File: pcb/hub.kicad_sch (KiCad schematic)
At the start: 0 parts

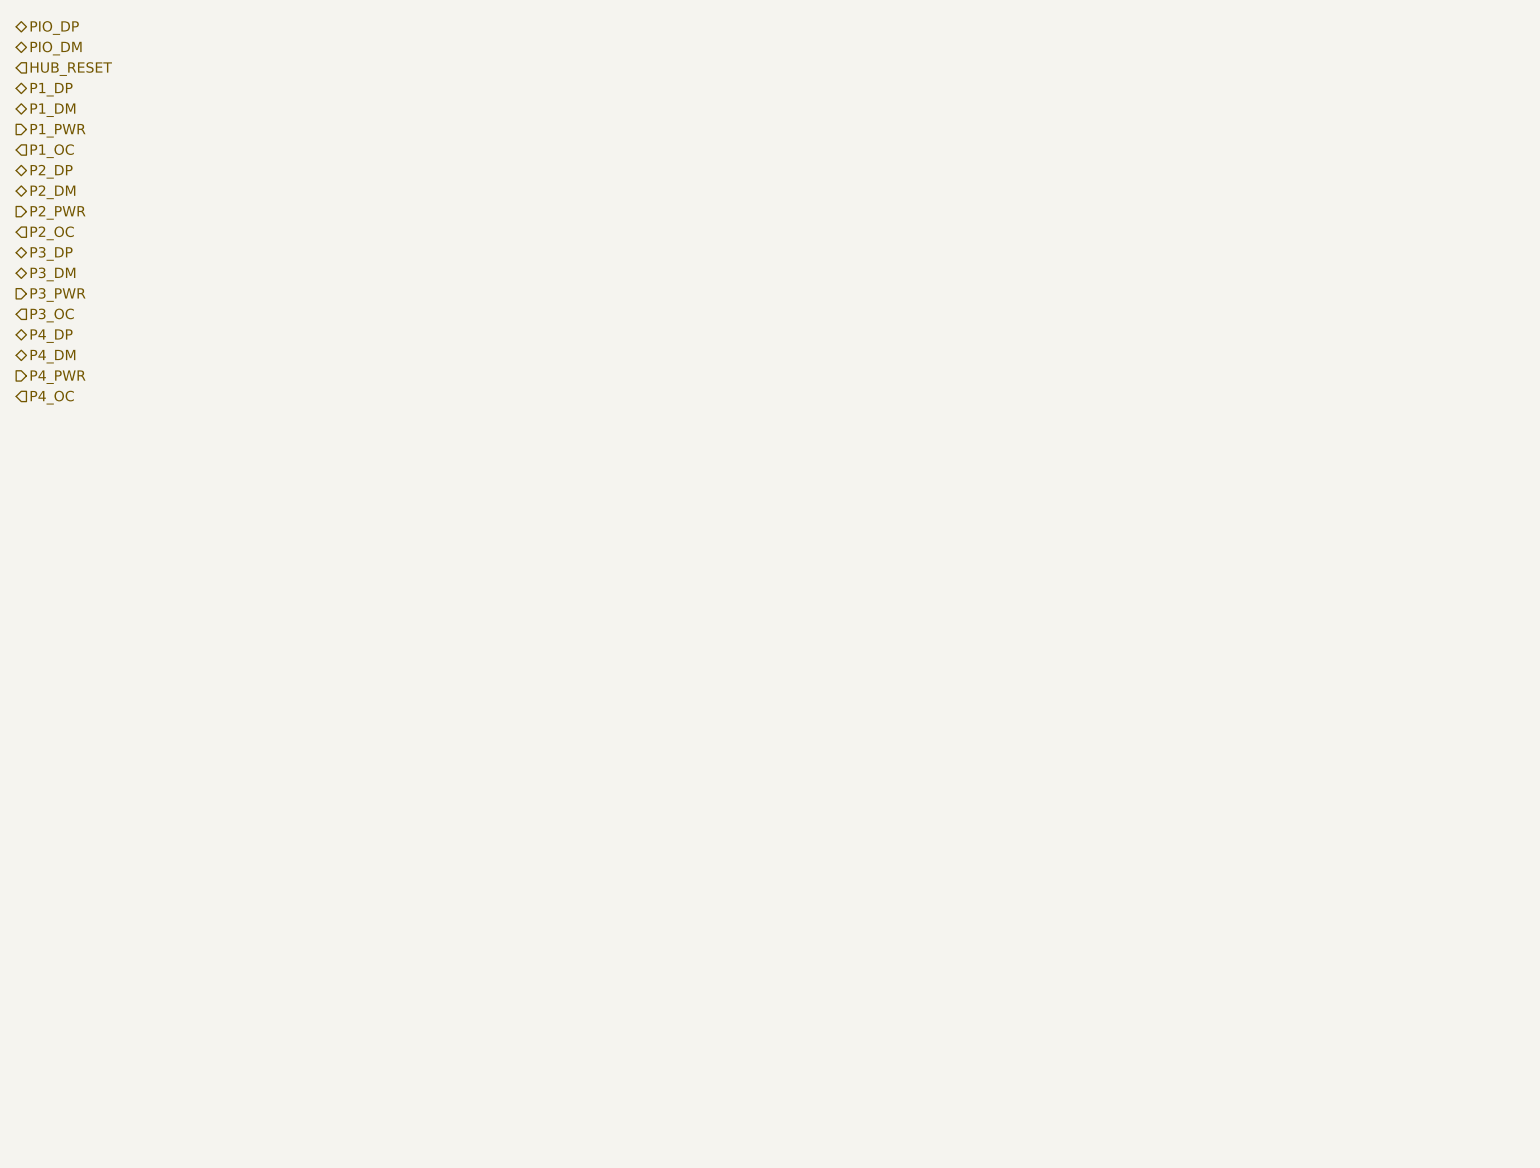
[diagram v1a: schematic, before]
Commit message: draw the hub sheet, with every passive turned side-on
The hub, its 24 MHz crystal, the RBIAS reference, both regulator filters, the
straps that select the default configuration, the reset and upstream-detect
pull-downs, and the upstream pair's series resistors with their host-side
pull-downs.

The thing that makes this sheet readable is that the passives are rotated. A
part standing upright has to be reached by a wire that leaves its pin's row, and
on a chip with fourteen pins down one side those wires cross each other and
everything else. Turned side-on, each passive sits in line with the pin it
serves: every pin owns a row and nothing crosses. The rotation convention was
measured out of KiCad rather than assumed -- a symbol turned 90 degrees puts a
pin at (X - py, Y - px), and the pin's own direction turns with it.

The datasheet settled what hangs off each pin. Both regulator filters take up to
0.1uF to ground or may be left unconnected. RBIAS takes 12.0k at 1%. TEST is to
be left alone -- no trace, no signal. And the two configuration-select pins are
strapped low through resistors rather than tied, because after reset they revert
to other functions, one of them an output.

HUB_VBUS_DET is plumbed through: a sheet pin on both blocks in the root, and on
the MCU sheet a pin that was spare now drives it.

Co-Authored-By: Claude Opus 5 (1M context) <noreply@anthropic.com>
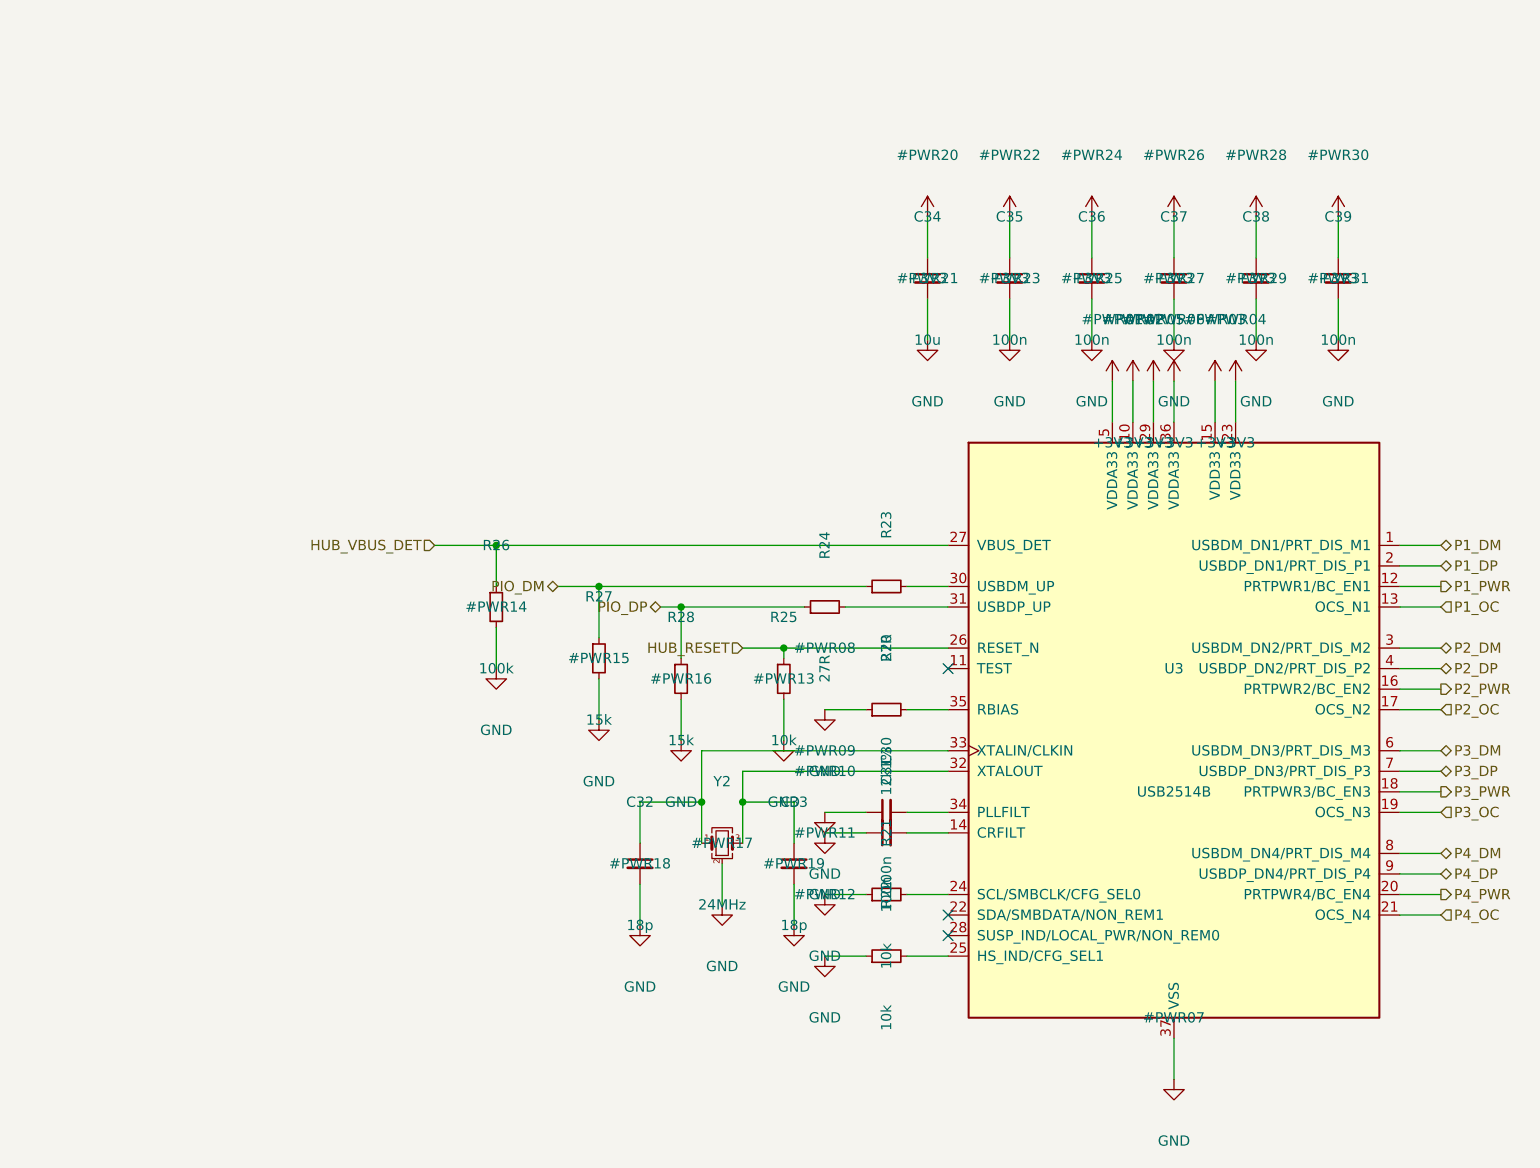
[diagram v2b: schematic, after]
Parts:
- added C30, C31, C35, C36, C37, C38, C39: 100n, symbol Device:C_Small
- added C32, C33: 18p, symbol Device:C_Small
- added C34: 10u, symbol Device:C_Small
- added R20: 12k1%, symbol Device:R_Small
- added R21, R22, R25: 10k, symbol Device:R_Small
- added R23, R24: 27R, symbol Device:R_Small
- added R26: 100k, symbol Device:R_Small
- added R27, R28: 15k, symbol Device:R_Small
- added U3: USB2514B, symbol Interface_USB:USB2514B_Bi
- added Y2: 24MHz, symbol Device:Crystal_GND24_Small
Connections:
- net HUB_RESET: now also R25.1, U3.26 (RESET_N)
- net P1_DM: now also U3.1 (USBDM_DN1/PRT_DIS_M1)
- net P1_DP: now also U3.2 (USBDP_DN1/PRT_DIS_P1)
- net P1_OC: now also U3.13 (OCS_N1)
- net P1_PWR: now also U3.12 (PRTPWR1/BC_EN1)
- net P2_DM: now also U3.3 (USBDM_DN2/PRT_DIS_M2)
- net P2_DP: now also U3.4 (USBDP_DN2/PRT_DIS_P2)
- net P2_OC: now also U3.17 (OCS_N2)
- net P2_PWR: now also U3.16 (PRTPWR2/BC_EN2)
- net P3_DM: now also U3.6 (USBDM_DN3/PRT_DIS_M3)
- net P3_DP: now also U3.7 (USBDP_DN3/PRT_DIS_P3)
- net P3_OC: now also U3.19 (OCS_N3)
- net P3_PWR: now also U3.18 (PRTPWR3/BC_EN3)
- net P4_DM: now also U3.8 (USBDM_DN4/PRT_DIS_M4)
- net P4_DP: now also U3.9 (USBDP_DN4/PRT_DIS_P4)
- net P4_OC: now also U3.21 (OCS_N4)
- net P4_PWR: now also U3.20 (PRTPWR4/BC_EN4)
- net PIO_DM: now also R23.1, R27.1
- net PIO_DP: now also R24.1, R28.1
- new net: C33.1, U3.32 (XTALOUT), Y2.3
- new net: C32.1, U3.33 (XTALIN/CLKIN), Y2.1
- new net: R21.2, U3.24 (SCL/SMBCLK/CFG_SEL0)
- new net: C30.2, U3.34 (PLLFILT)
- new net: R24.2, U3.31 (USBDP_UP)
- new net: R22.2, U3.25 (HS_IND/CFG_SEL1)
- new net: C31.2, U3.14 (CRFILT)
- new net: R23.2, U3.30 (USBDM_UP)
- new net: R20.2, U3.35 (RBIAS)
- new net +3V3: C34.1, C35.1, C36.1, C37.1, C38.1, C39.1, U3.10 (VDDA33), U3.15 (VDD33), U3.23 (VDD33), U3.29 (VDDA33), U3.36 (VDDA33), U3.5 (VDDA33)
- new net GND: C30.1, C31.1, C32.2, C33.2, C34.2, C35.2, C36.2, C37.2, C38.2, C39.2, R20.1, R21.1, R22.1, R25.2, R26.2, R27.2, R28.2, U3.37 (VSS), Y2.2 (G), Y2.4 (G)
- new net HUB_VBUS_DET: R26.1, U3.27 (VBUS_DET)
- no-connect marks 0 -> 3

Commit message: hide the power symbols' references on the hub sheet
A power symbol's reference has to be unique so the sheet can be annotated, but
it is not meant to be read off the drawing, and thirty-odd of them printed over
the parts is just noise. The value stays visible, because on a power symbol the
value is the net name -- which is the part anyone actually wants to see.

Done as a pass over the finished file rather than inline in the symbol writer:
the escaping needed to emit a conditional line from inside a printf format was
where the last attempt went wrong, and a second pass over a file that already
parses is both simpler and easier to check. The generator now runs it, so the
sheets still to be drawn will not need the same correction.

Co-Authored-By: Claude Opus 5 (1M context) <noreply@anthropic.com>
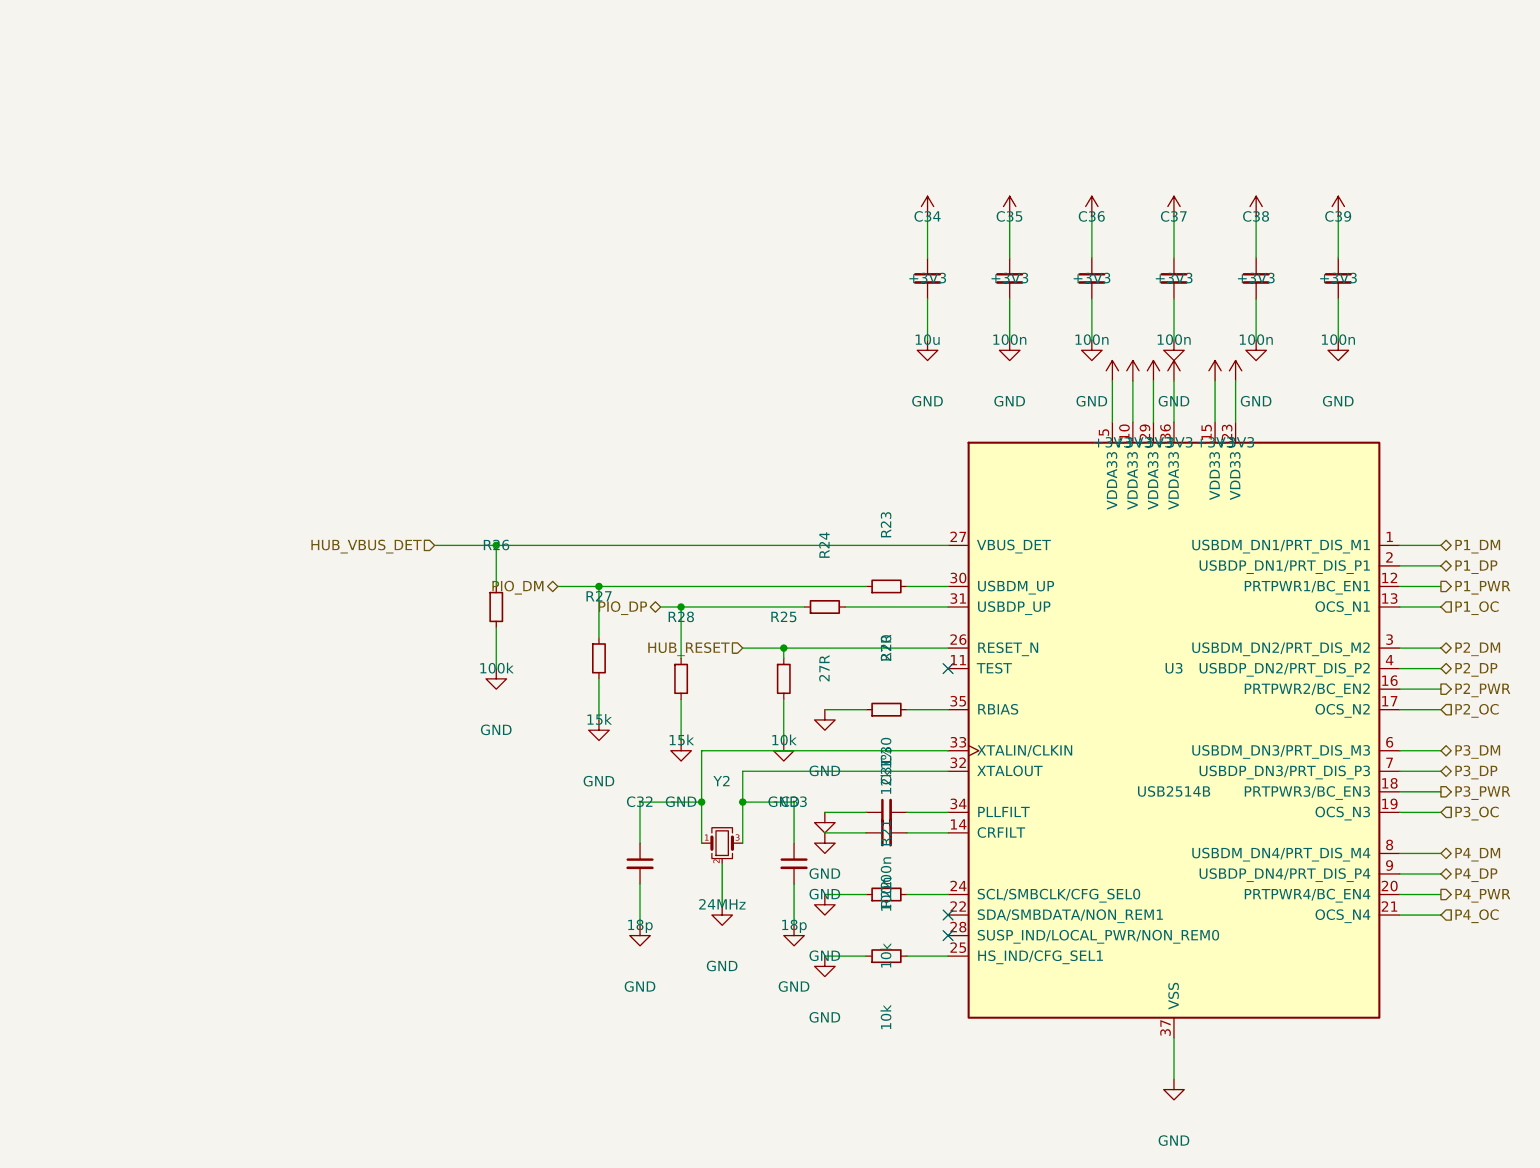
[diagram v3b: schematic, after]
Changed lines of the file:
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@@
 		(property "Reference" "#PWR01"
 			(at 195.58 76.20 0)
+			(hide yes)
 			(effects
 				(font
@@
 		(property "Reference" "#PWR02"
 			(at 198.12 76.20 0)
+			(hide yes)
 			(effects
 				(font
@@
 		(property "Reference" "#PWR03"
 			(at 208.28 76.20 0)
+			(hide yes)
 			(effects
 				(font
@@
 		(property "Reference" "#PWR04"
 			(at 210.82 76.20 0)
+			(hide yes)
 			(effects
 				(font
@@
 		(property "Reference" "#PWR05"
 			(at 200.66 76.20 0)
+			(hide yes)
 			(effects
 				(font
@@
 		(property "Reference" "#PWR06"
 			(at 203.20 76.20 0)
+			(hide yes)
 			(effects
 				(font
@@
 		(property "Reference" "#PWR07"
 			(at 203.20 162.56 0)
+			(hide yes)
 			(effects
 				(font
@@
 		(property "Reference" "#PWR08"
 			(at 160.02 116.84 0)
+			(hide yes)
 			(effects
 				(font
@@
 		(property "Reference" "#PWR09"
 			(at 160.02 129.54 0)
+			(hide yes)
 			(effects
 				(font
@@
 		(property "Reference" "#PWR10"
 			(at 160.02 132.08 0)
+			(hide yes)
 			(effects
 				(font
@@
 		(property "Reference" "#PWR11"
 			(at 160.02 139.70 0)
+			(hide yes)
 			(effects
 				(font
@@
 		(property "Reference" "#PWR12"
 			(at 160.02 147.32 0)
+			(hide yes)
 			(effects
 				(font
@@
 		(property "Reference" "#PWR13"
 			(at 154.94 120.65 0)
+			(hide yes)
 			(effects
 				(font
@@
 		(property "Reference" "#PWR14"
 			(at 119.38 111.76 0)
+			(hide yes)
 			(effects
 				(font
@@
 		(property "Reference" "#PWR15"
 			(at 132.08 118.11 0)
+			(hide yes)
 			(effects
 				(font
@@
 		(property "Reference" "#PWR16"
 			(at 142.24 120.65 0)
+			(hide yes)
 			(effects
 				(font
@@
 		(property "Reference" "#PWR17"
 			(at 147.32 140.97 0)
+			(hide yes)
 			(effects
 				(font
@@
 		(property "Reference" "#PWR18"
 			(at 137.16 143.51 0)
+			(hide yes)
 			(effects
 				(font
@@
 		(property "Reference" "#PWR19"
 			(at 156.21 143.51 0)
+			(hide yes)
 			(effects
 				(font
@@
 		(property "Reference" "#PWR20"
 			(at 172.72 55.88 0)
+			(hide yes)
 			(effects
 				(font
@@
 		(property "Reference" "#PWR21"
 			(at 172.72 71.12 0)
+			(hide yes)
 			(effects
 				(font
@@
 		(property "Reference" "#PWR22"
 			(at 182.88 55.88 0)
+			(hide yes)
 			(effects
 				(font
@@
 		(property "Reference" "#PWR23"
 			(at 182.88 71.12 0)
+			(hide yes)
 			(effects
 				(font
@@
 		(property "Reference" "#PWR24"
 			(at 193.04 55.88 0)
+			(hide yes)
 			(effects
 				(font
@@
 		(property "Reference" "#PWR25"
 			(at 193.04 71.12 0)
+			(hide yes)
 			(effects
 				(font
@@
 		(property "Reference" "#PWR26"
 			(at 203.20 55.88 0)
+			(hide yes)
 			(effects
 				(font
@@
 		(property "Reference" "#PWR27"
 			(at 203.20 71.12 0)
+			(hide yes)
 			(effects
 				(font
@@
 		(property "Reference" "#PWR28"
 			(at 213.36 55.88 0)
+			(hide yes)
 			(effects
 				(font
@@
 		(property "Reference" "#PWR29"
 			(at 213.36 71.12 0)
+			(hide yes)
 			(effects
 				(font
@@
 		(property "Reference" "#PWR30"
 			(at 223.52 55.88 0)
+			(hide yes)
 			(effects
 				(font
@@
 		(property "Reference" "#PWR31"
 			(at 223.52 71.12 0)
-			(effects
-				(font
+			(hide yes)
+			(effects
+				(font
